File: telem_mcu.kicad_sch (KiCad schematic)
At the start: 32 parts, among them J3 JTAG, SW2 SW_Push, SW3 SW_SPDT, U3 STM32F373CCTx, X1 32.768kHz, Y1 8MHz

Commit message: Added MAX-M10S GPS, selected antenna and did schematic
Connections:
- net GPS_TP: now reaches U3.19 (PB1)
- net GPS_SCL: now reaches U3.30 (PA9)
- net GPS_SDA: now reaches U3.31 (PA10)
- net GPS_RST: now reaches U3.41 (PB5)
- no-connect marks 17 -> 13
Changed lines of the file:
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@@
-	)
-	(no_connect
-		(at 163.83 114.3)
 	)
 	(no_connect
@@
 	)
 	(no_connect
-		(at 163.83 83.82)
-	)
-	(no_connect
-		(at 163.83 104.14)
-	)
-	(no_connect
 		(at 123.19 88.9)
 	)
@@
 	)
 	(no_connect
-		(at 163.83 81.28)
-	)
-	(no_connect
 		(at 123.19 101.6)
 	)
@@
 	(wire
 		(pts
+			(xy 163.83 114.3) (xy 168.91 114.3)
+		)
+		(stroke
+			(width 0)
+			(type default)
+		)
+	)
+	(wire
+		(pts
 			(xy 147.32 176.53) (xy 161.29 176.53)
 		)
@@
 	(wire
 		(pts
+			(xy 163.83 83.82) (xy 168.91 83.82)
+		)
+		(stroke
+			(width 0)
+			(type default)
+		)
+	)
+	(wire
+		(pts
 			(xy 140.97 139.7) (xy 143.51 139.7)
 		)
@@
 	(wire
 		(pts
+			(xy 163.83 104.14) (xy 168.91 104.14)
+		)
+		(stroke
+			(width 0)
+			(type default)
+		)
+	)
+	(wire
+		(pts
 			(xy 143.51 50.8) (xy 140.97 50.8)
 		)
@@
 		(pts
 			(xy 106.68 111.76) (xy 110.49 111.76)
+		)
+		(stroke
+			(width 0)
+			(type default)
+		)
+	)
+	(wire
+		(pts
+			(xy 163.83 81.28) (xy 168.91 81.28)
 		)
 		(stroke
@@
 			)
 			(justify left bottom)
+		)
+	)
+	(hierarchical_label "GPS_SDA"
+		(shape output)
+		(at 168.91 83.82 0)
+		(effects
+			(font
+				(size 1.27 1.27)
+			)
+			(justify left)
 		)
 	)
@@
 		)
 	)
+	(hierarchical_label "GPS_SCL"
+		(shape input)
+		(at 168.91 81.28 0)
+		(effects
+			(font
+				(size 1.27 1.27)
+			)
+			(justify left)
+		)
+	)
 	(hierarchical_label "BMP_SCX"
 		(shape output)
@@
 		)
 	)
+	(hierarchical_label "GPS_RST"
+		(shape output)
+		(at 168.91 114.3 0)
+		(effects
+			(font
+				(size 1.27 1.27)
+			)
+			(justify left)
+		)
+	)
 	(hierarchical_label "IMU_SPC"
 		(shape output)
@@
 		(effects
 			(font
+				(size 1.27 1.27)
+			)
+			(justify left)
+		)
+	)
+	(hierarchical_label "GPS_TP"
+		(shape input)
+		(at 168.91 104.14 0)
+		(effects
+			(font

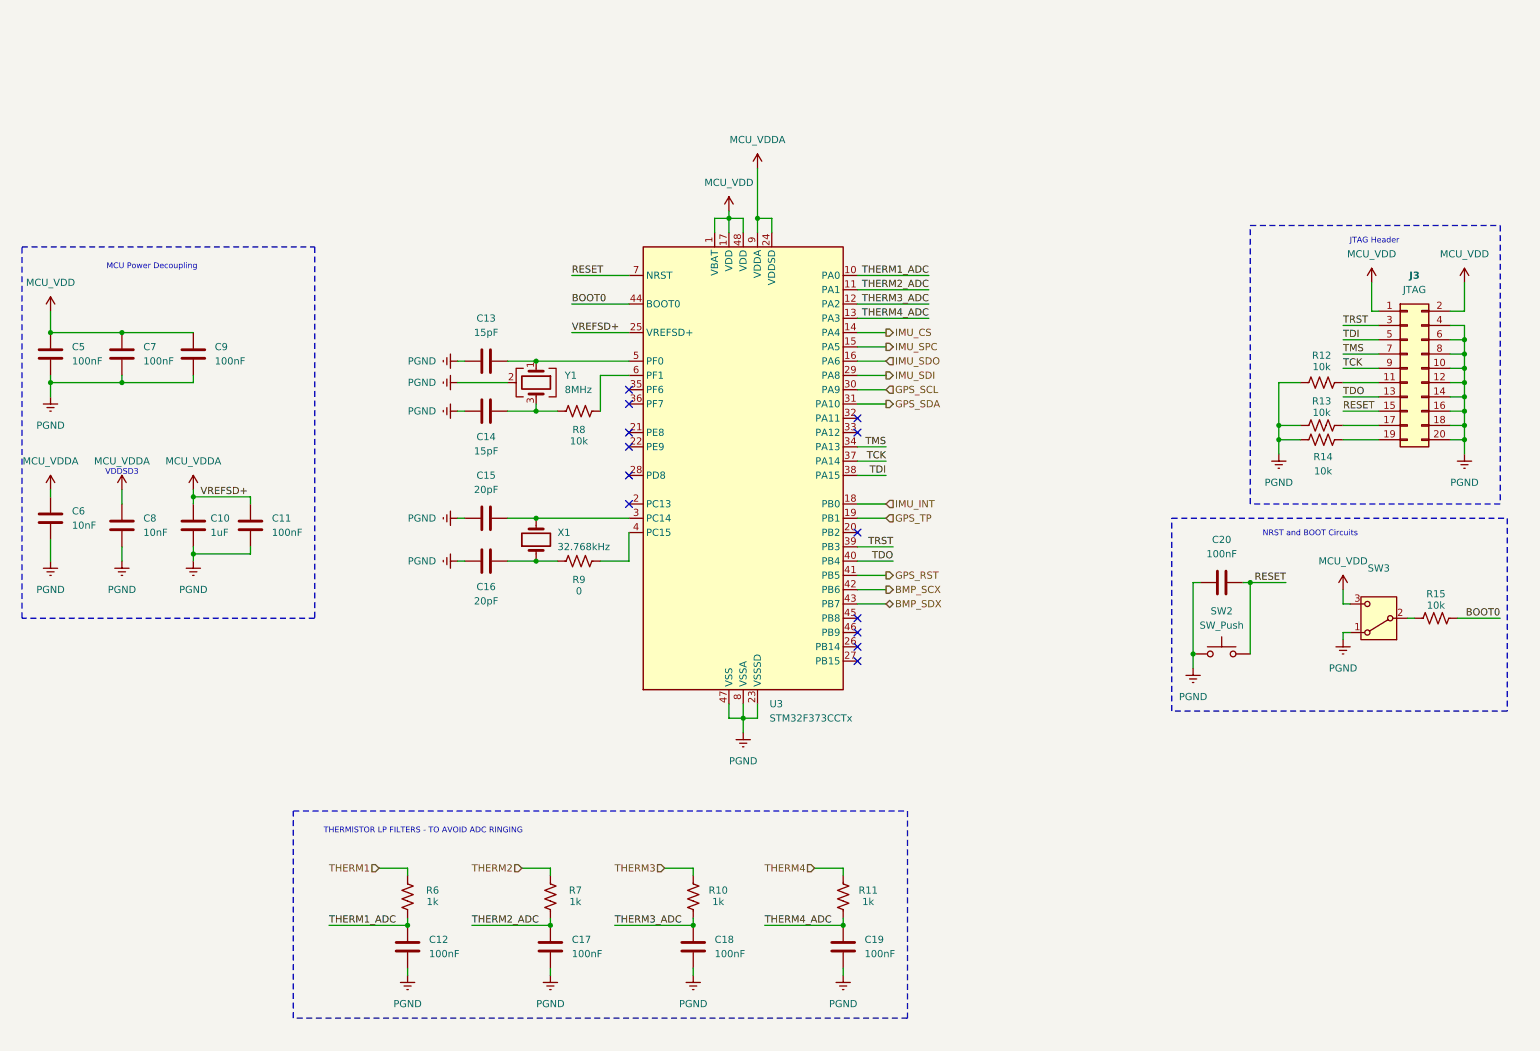
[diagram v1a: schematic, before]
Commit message: Schematics complete; Starting layout. Removed 2 thermistors, not necessary. Going to update website once layout starts
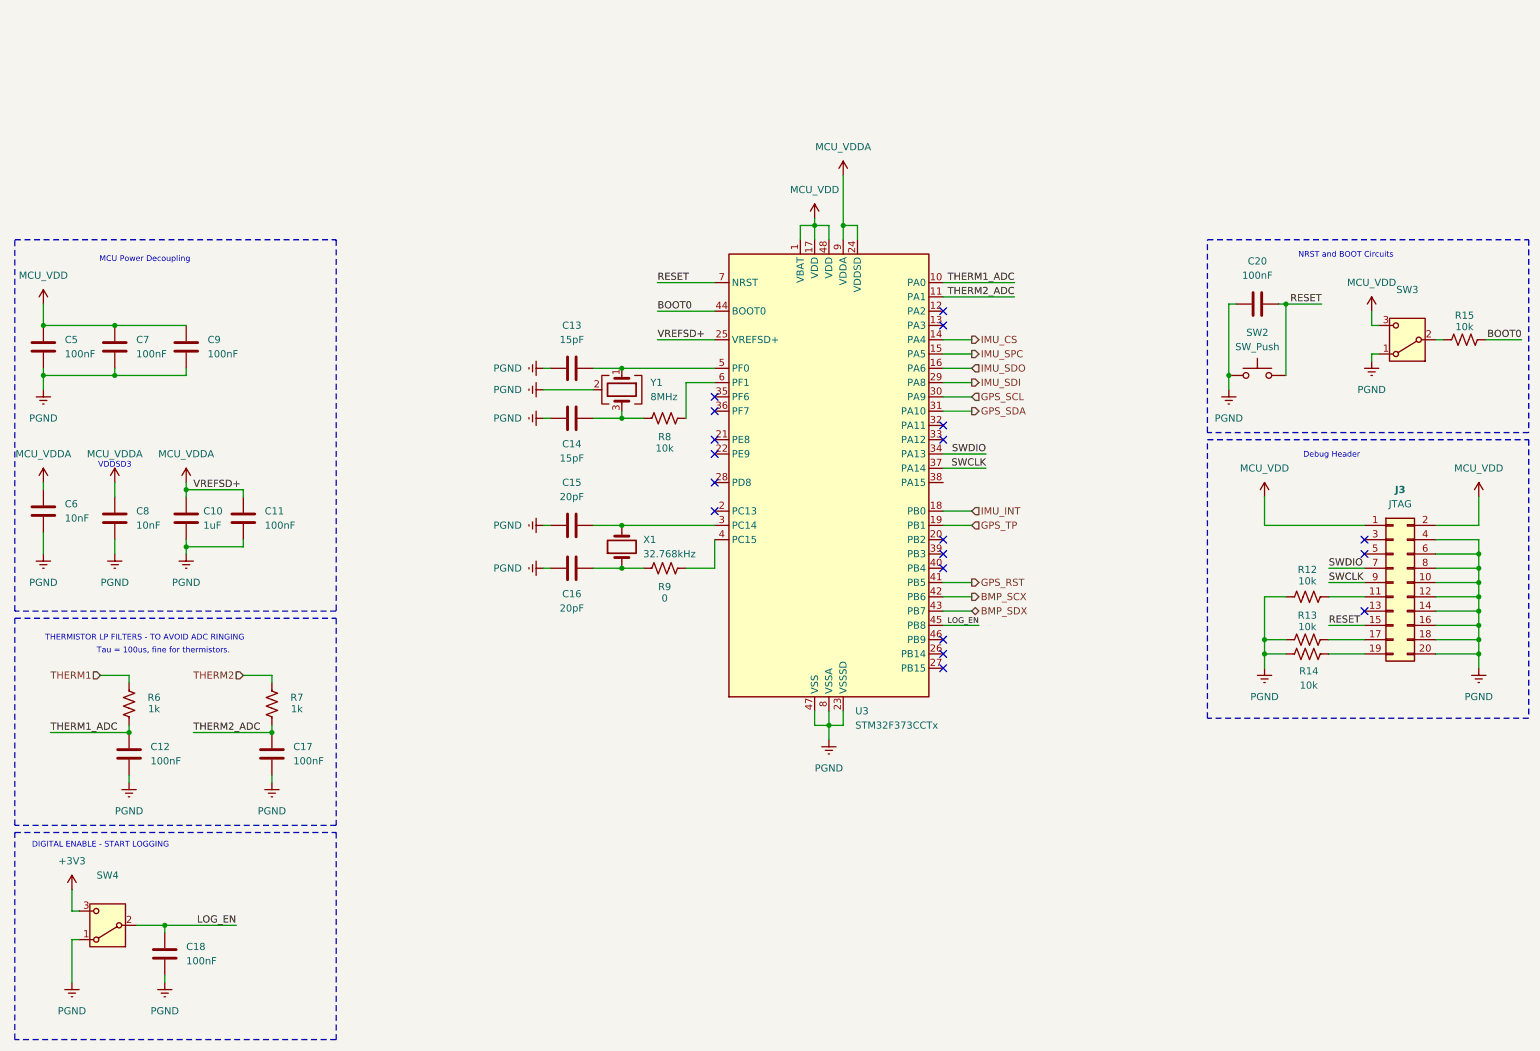
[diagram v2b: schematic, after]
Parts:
- removed C19: 100nF, Capacitor_SMD:C_0805_2012Metric_Pad1.18x1.45mm_HandSolder, symbol Device:C
- removed R10, R11: 1k, Resistor_SMD:R_0603_1608Metric, symbol Device:R_US
- added SW4: SW_SPDT, Telem_fp:CL-SB-12B-02T_NDC, symbol Switch:SW_SPDT
- C18: footprint Capacitor_SMD:C_0805_2012Metric_Pad1.18x1.45mm_HandSolder -> Capacitor_SMD:C_0603_1608Metric
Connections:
- net PGND: now also SW4.1 (A)
- net LOG_EN: now reaches U3.45 (PB8)
- net LOG_EN: now also C18.1, SW4.2 (B)
- net TCK renamed SWCLK
- net TDI: no longer names the net of J3.5 (Pin_5)
- net TDI: no longer U3.38 (PA15)
- net TDO: no longer names the net of J3.13 (Pin_13)
- net TDO: no longer U3.40 (PB4)
- net THERM3_ADC: no longer names the net of U3.12 (PA2)
- net THERM3_ADC: no longer C18.1
- net THERM4_ADC: no longer names the net of U3.13 (PA3)
- net TMS renamed SWDIO
- net TRST: no longer names the net of J3.3 (Pin_3)
- net TRST: no longer U3.39 (PB3)
- new net +3V3: SW4.3 (C)
- no-connect marks 13 -> 19
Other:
- note added: "DIGITAL ENABLE - START LOGGING"
- note added: "Debug Header"
- note added: "Tau = 100us, fine for thermistors."
- note removed: "JTAG Header"
- moved on the sheet: C10, C11, C12, C13, C14, C15, C16, C17, C20, C5, C6, C7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

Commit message: Final schematic and initial layout
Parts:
- removed C18: 100nF, Capacitor_SMD:C_0603_1608Metric, symbol Device:C
- removed R12, R13, R14: 10k, Resistor_SMD:R_0603_1608Metric, symbol Device:R_US
- removed SW4: SW_SPDT, Telem_fp:CL-SB-12B-02T_NDC, symbol Switch:SW_SPDT
- C12, C17: footprint Capacitor_SMD:C_0805_2012Metric_Pad1.18x1.45mm_HandSolder -> Capacitor_SMD:C_0805_2012Metric
- SW3: footprint Telem_fp:CL-SB-12B-02T_NDC -> Telem_fp:SWITCH_1SCQN
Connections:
- no-connect marks 19 -> 22
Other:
- note removed: "DIGITAL ENABLE - START LOGGING"

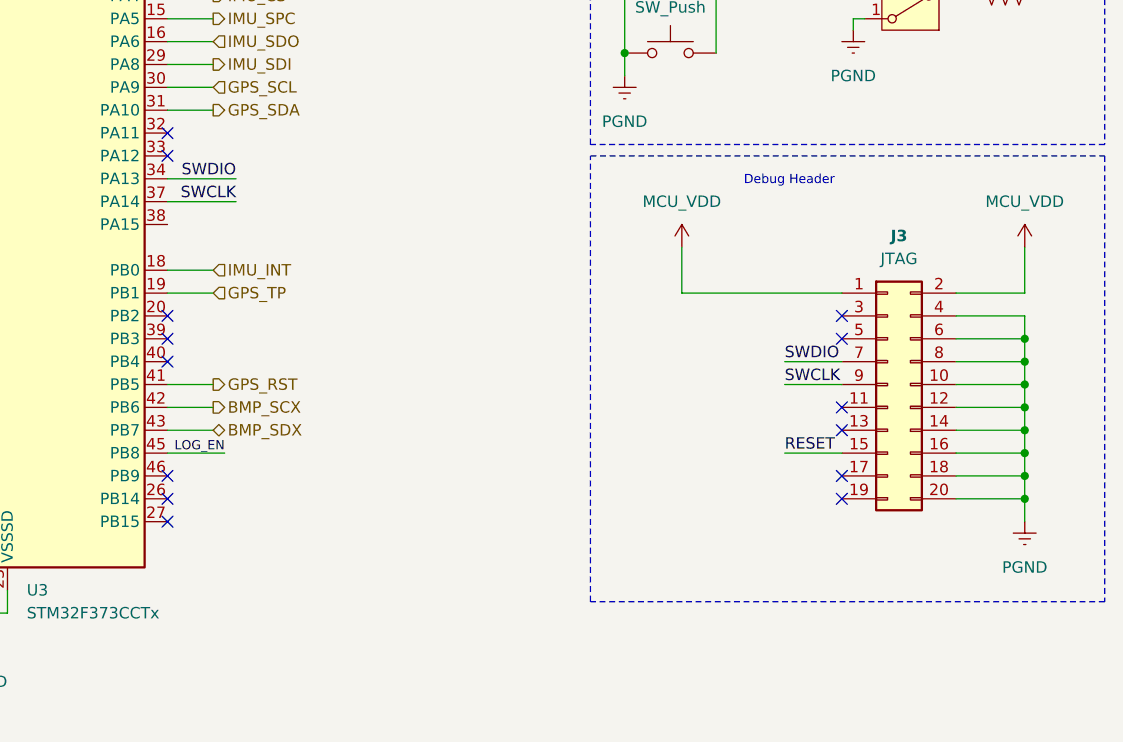
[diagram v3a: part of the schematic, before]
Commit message: Finished initial signal layout
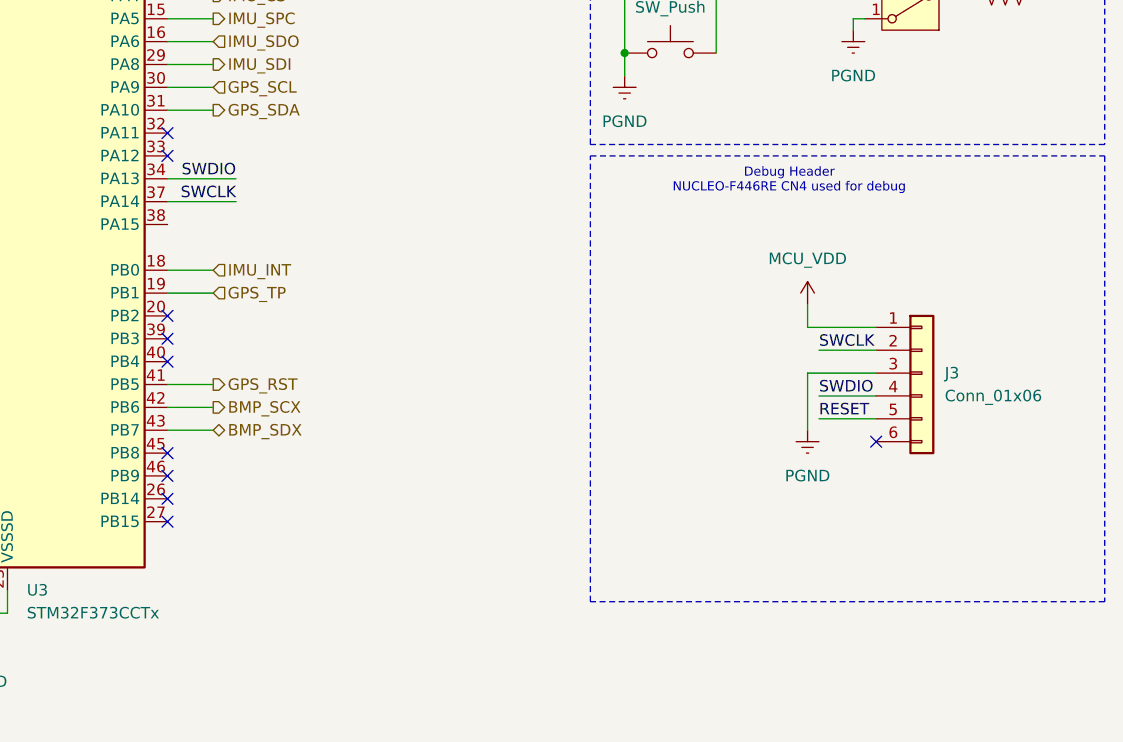
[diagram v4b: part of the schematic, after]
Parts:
- removed J3: JTAG, Connector_PinSocket_2.54mm:PinSocket_2x10_P2.54mm_Vertical_SMD, symbol Connector_Generic:Conn_02x10_Odd_Even
- added J3: Conn_01x06, Connector_PinHeader_2.54mm:PinHeader_1x06_P2.54mm_Vertical_SMD_Pin1Right, symbol Connector_Generic:Conn_01x06
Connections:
- net MCU_VDD: now also J3.1 (Pin_1)
- net PGND: now also J3.3 (Pin_3)
- net RESET: now also J3.5 (Pin_5)
- net SWCLK: now also J3.2 (Pin_2)
- net SWDIO: now also J3.4 (Pin_4)
- net LOG_EN: no longer names the net of U3.45 (PB8)
- no-connect marks 22 -> 18
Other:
- note added: "Debug Header NUCLEO-F446RE CN4 used for debug"
- note removed: "Debug Header"

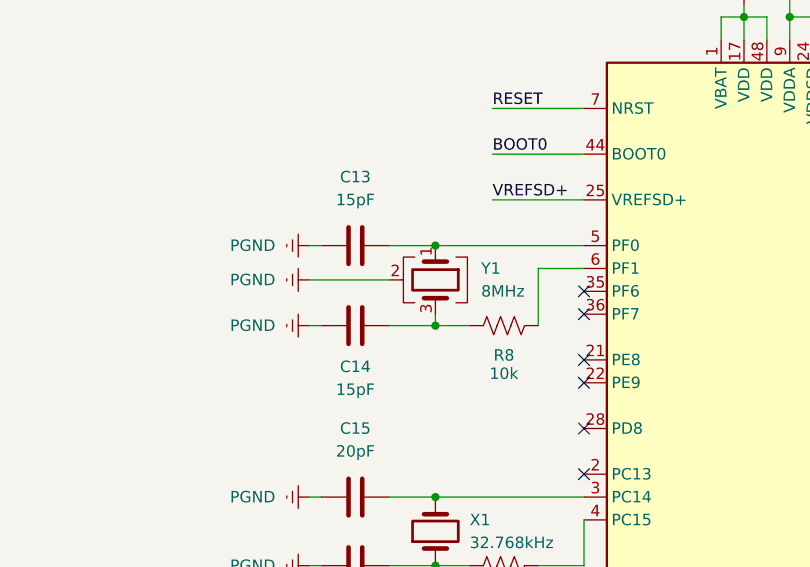
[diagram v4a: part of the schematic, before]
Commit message: Removed 8Mhz Crystal. Not necessary, not using 72MHz. Also simplifies routing
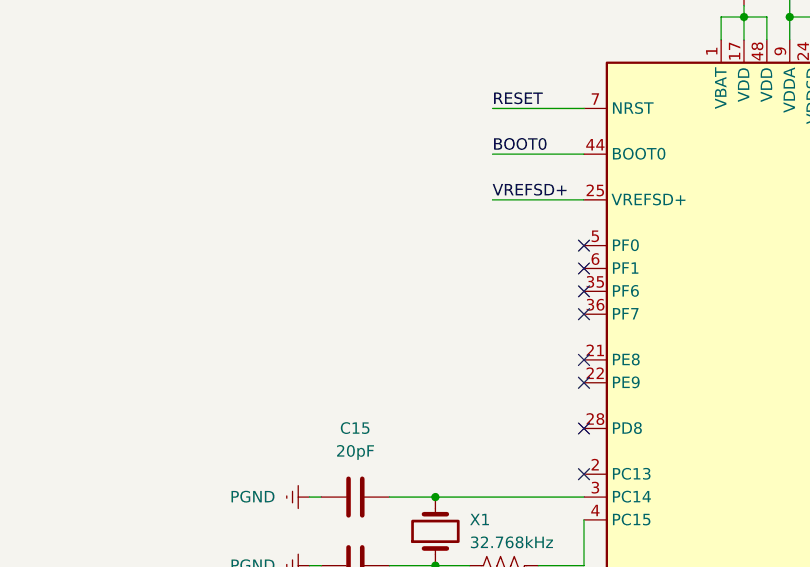
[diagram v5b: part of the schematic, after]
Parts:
- removed C13, C14: 15pF, Capacitor_SMD:C_0603_1608Metric, symbol Device:C
- removed R8: 10k, Resistor_SMD:R_0603_1608Metric, symbol Device:R_US
- removed Y1: 8MHz, Crystal:Crystal_SMD_5032-4Pin_5.0x3.2mm, symbol Device:Crystal_GND24
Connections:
- no-connect marks 18 -> 20
